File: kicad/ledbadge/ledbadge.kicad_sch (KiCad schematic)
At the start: 3 parts

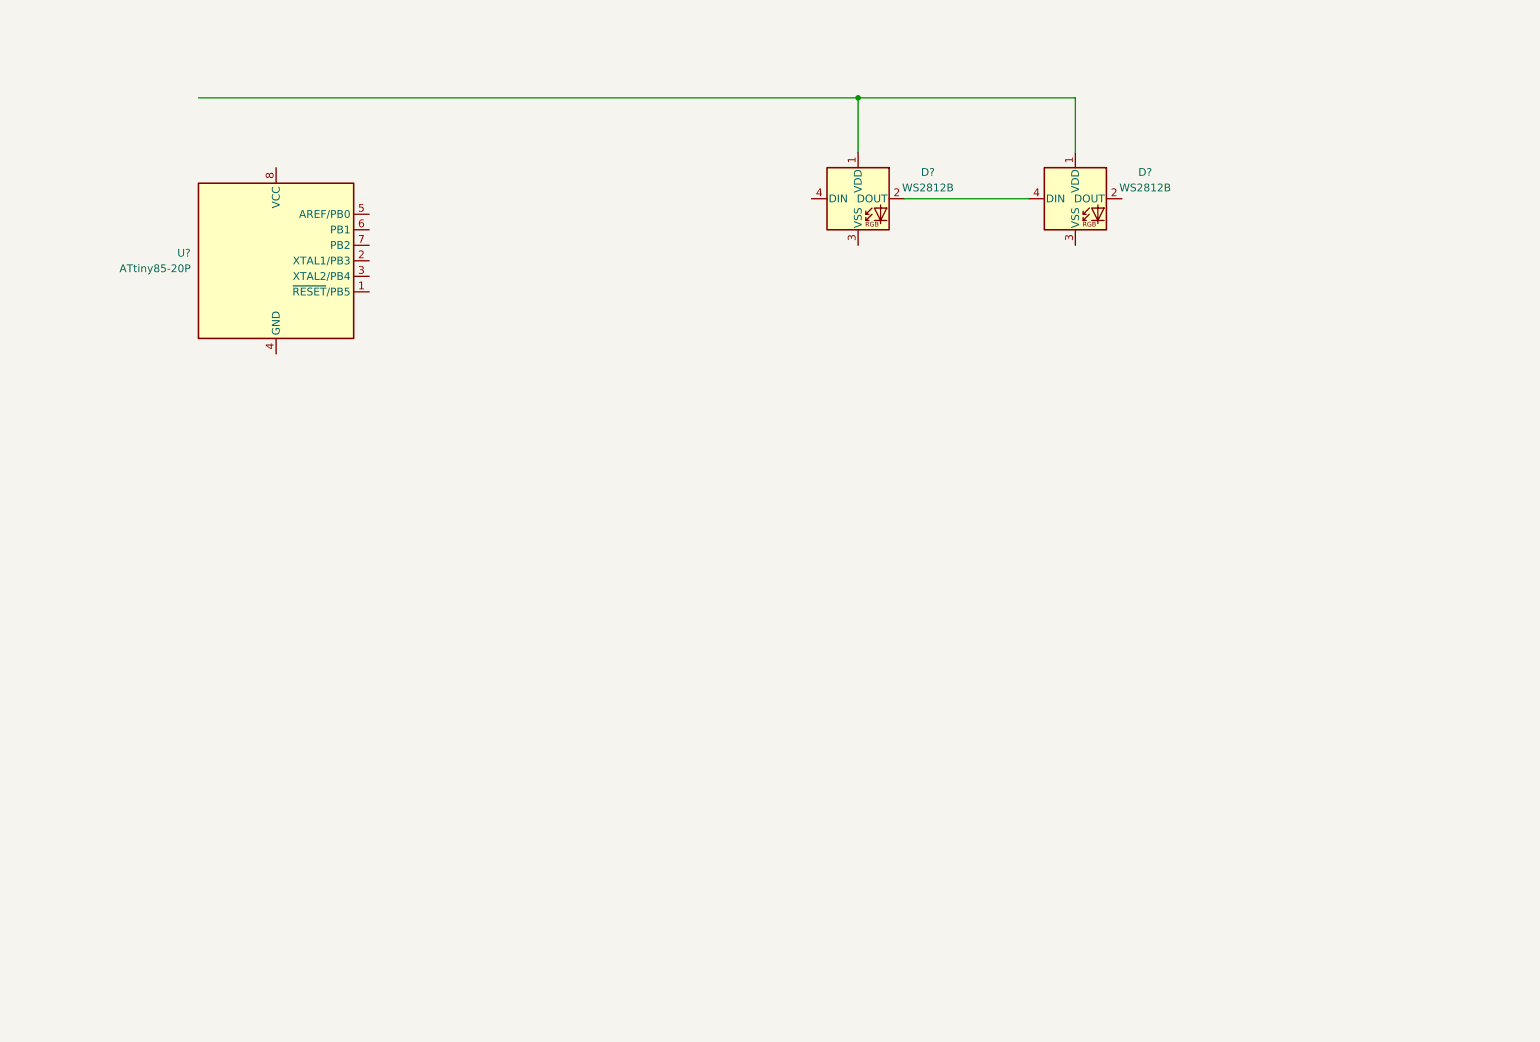
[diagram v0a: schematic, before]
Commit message: add a few more symbols, tidy up basic Readme added bypass capacitors and power symbols to the schematic
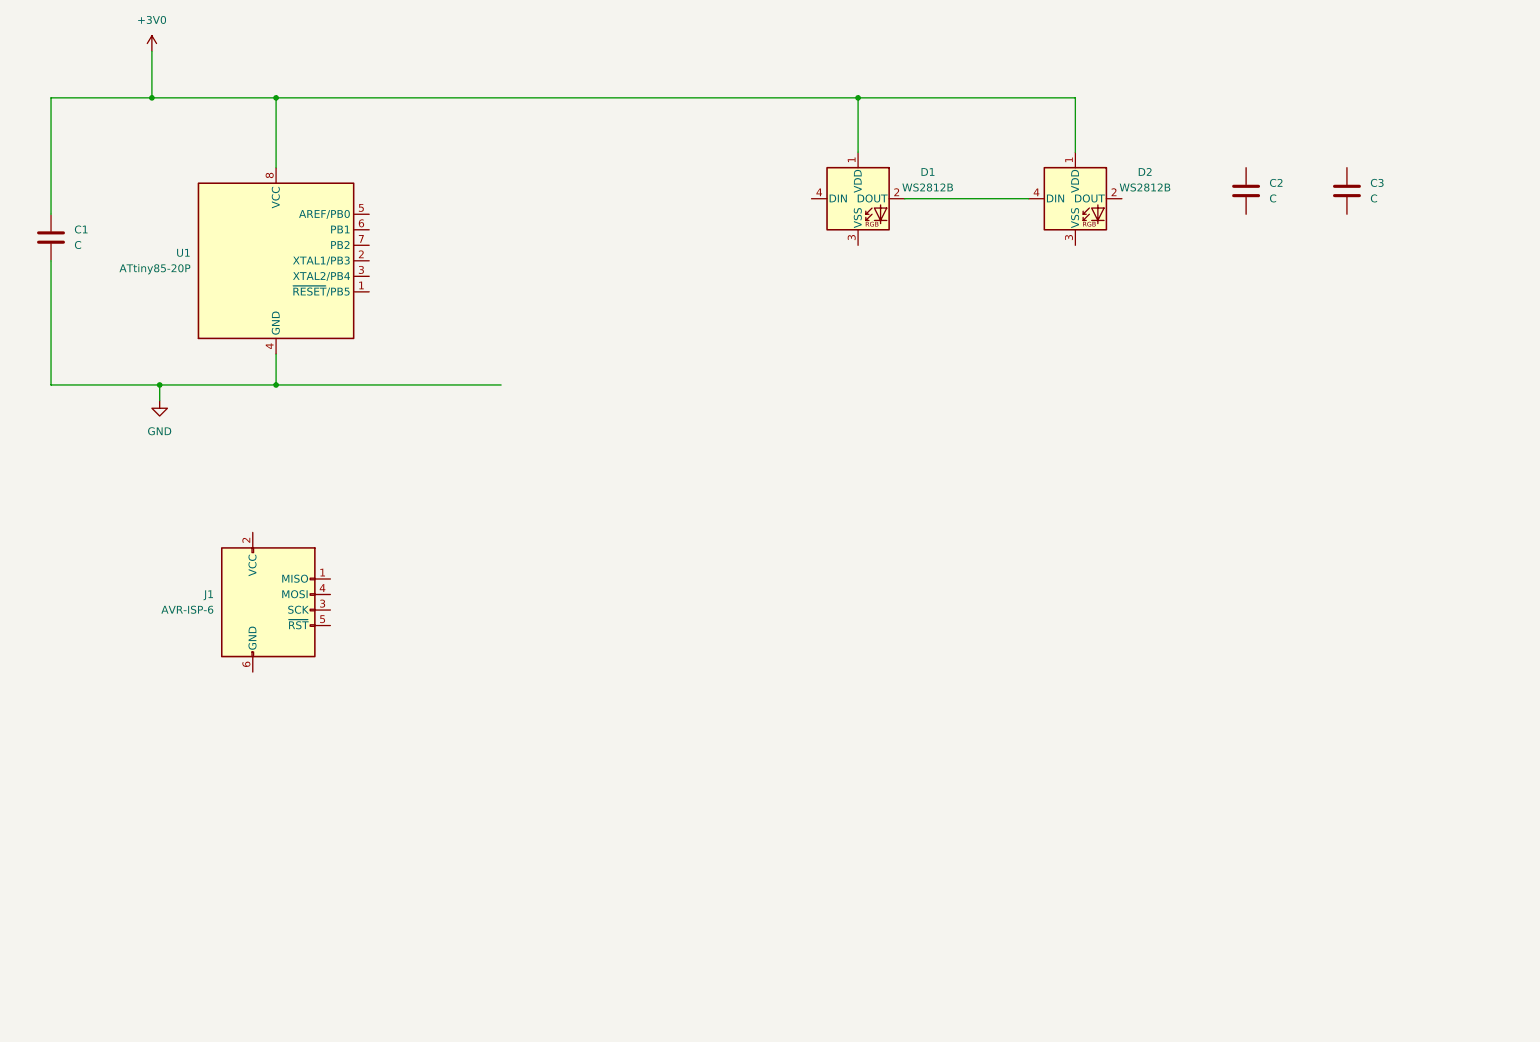
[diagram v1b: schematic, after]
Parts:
- added C1, C2, C3: C, symbol Device:C
- added J1: AVR-ISP-6, symbol Connector:AVR-ISP-6
- gave numbers to parts that had none: 3
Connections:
- net +3V0: now reaches D1.1 (VDD), D2.1 (VDD)
- net +3V0: now also U1.8 (VCC), C1.1
- net GND: now reaches U1.4 (GND)
- net GND: now also C1.2

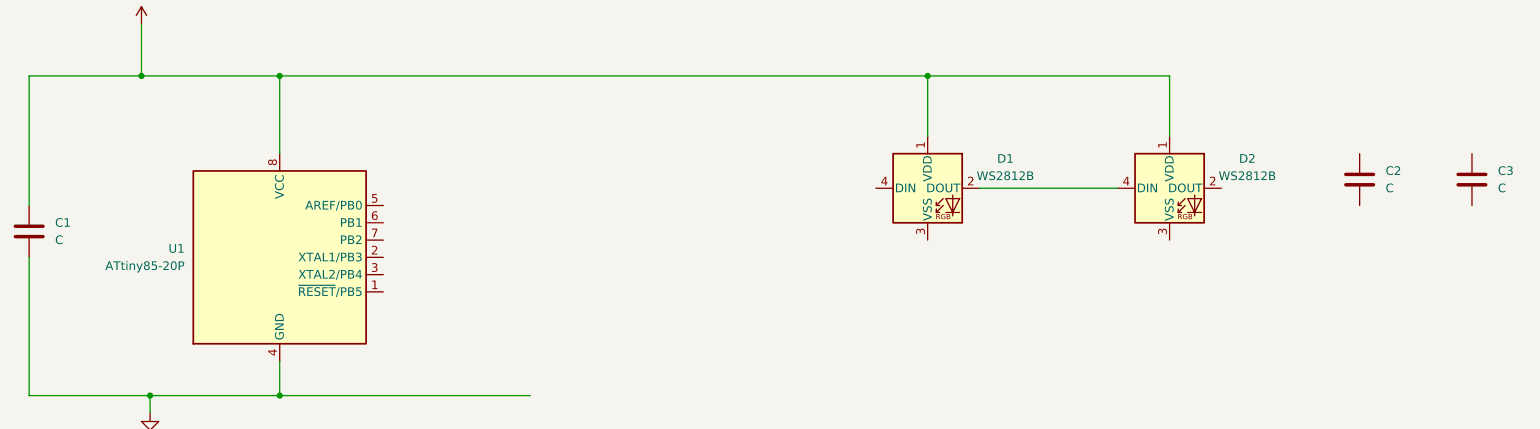
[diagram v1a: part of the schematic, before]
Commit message: add values to capacitors
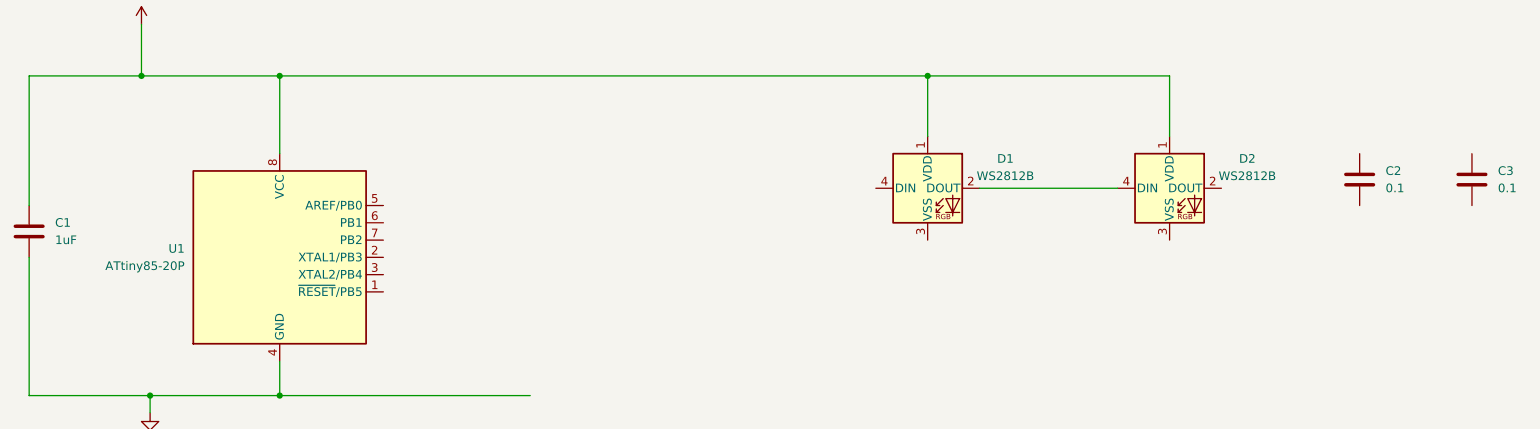
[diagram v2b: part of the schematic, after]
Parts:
- C1: value C -> 1uF
- C2, C3: value C -> 0.1
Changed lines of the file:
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@@
       (effects (font (size 1.27 1.27)) (justify left))
     )
-    (property "Value" "C" (at 231.14 57.15 0)
+    (property "Value" "0.1" (at 231.14 57.15 0)
       (effects (font (size 1.27 1.27)) (justify left))
     )
@@
       (effects (font (size 1.27 1.27)) (justify left))
     )
-    (property "Value" "C" (at 247.65 57.15 0)
+    (property "Value" "0.1" (at 247.65 57.15 0)
       (effects (font (size 1.27 1.27)) (justify left))
     )
@@
       (effects (font (size 1.27 1.27)) (justify left))
     )
-    (property "Value" "C" (at 35.56 64.77 0)
+    (property "Value" "1uF" (at 35.56 64.77 0)
       (effects (font (size 1.27 1.27)) (justify left))
     )

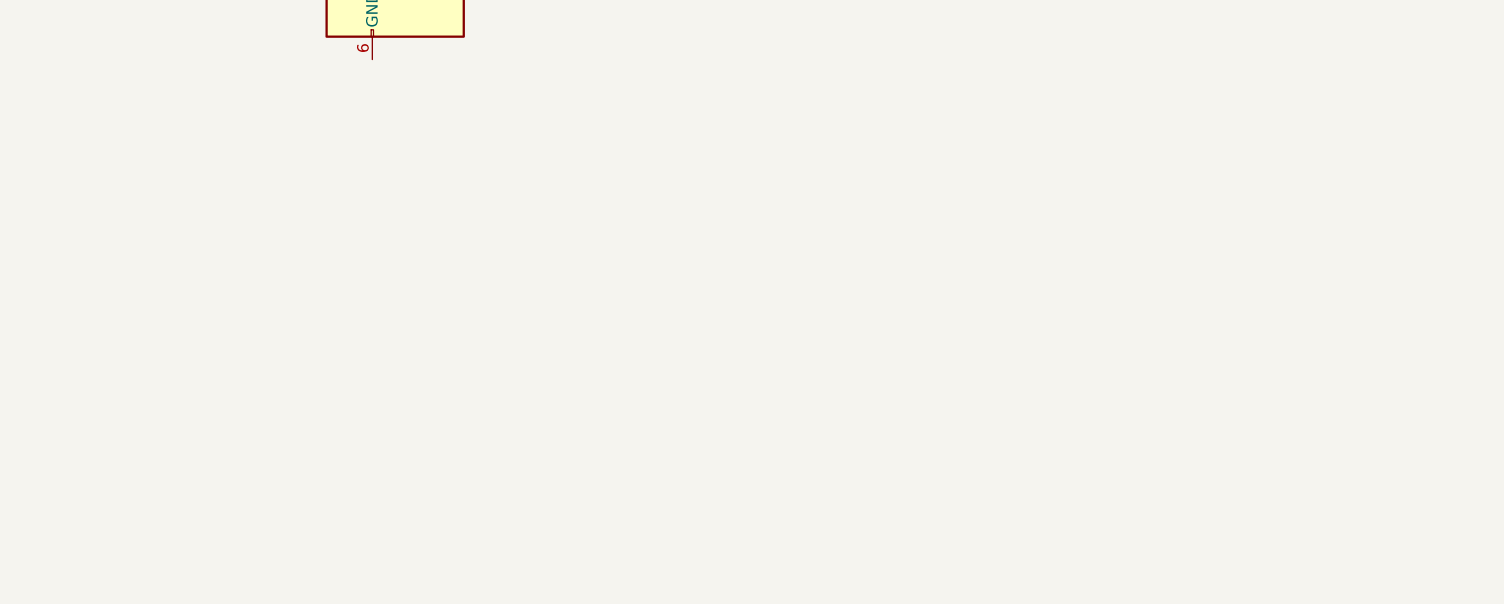
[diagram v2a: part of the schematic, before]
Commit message: add power input parts: battery, power switch
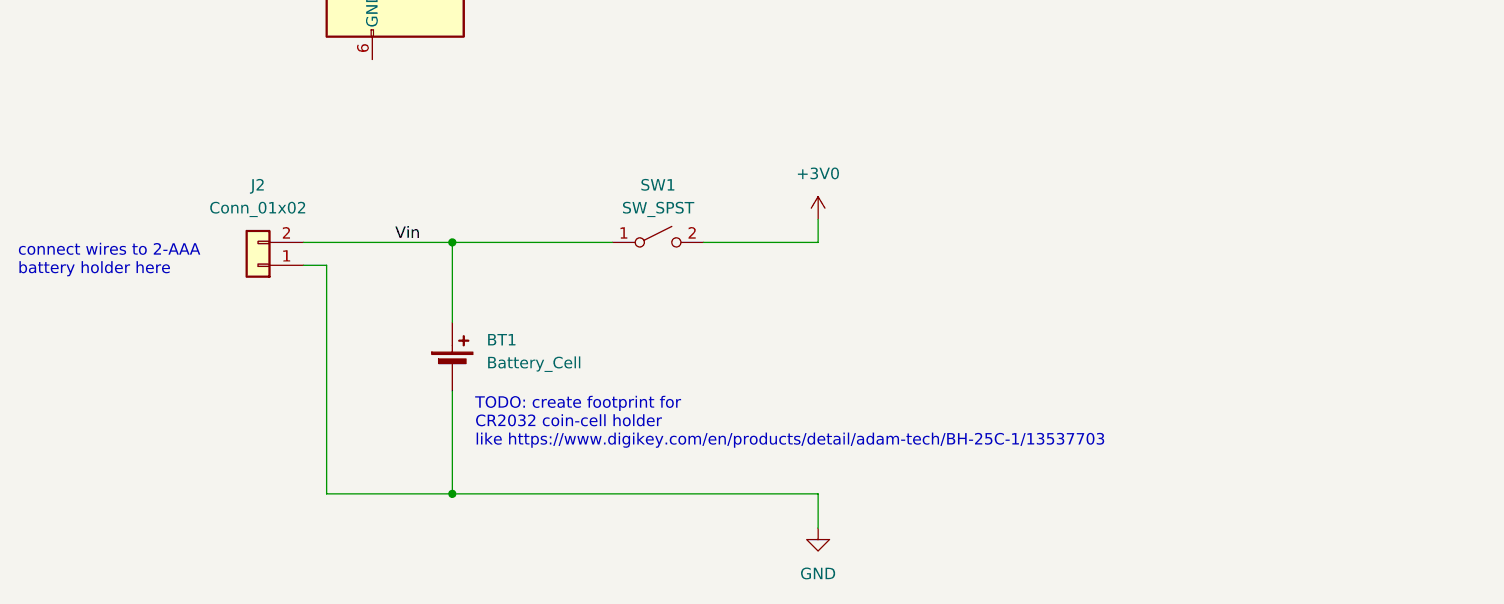
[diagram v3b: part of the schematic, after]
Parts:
- added BT1: Battery_Cell, symbol Device:Battery_Cell
- added J2: Conn_01x02, symbol Connector_Generic:Conn_01x02
- added SW1: SW_SPST, symbol Switch:SW_SPST
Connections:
- net +3V0: now also SW1.2 (B)
- net GND: now also BT1.2 (-), J2.1 (Pin_1)
- new net Vin: BT1.1 (+), J2.2 (Pin_2), SW1.1 (A)
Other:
- note added: "TODO: create footprint for CR2032 coin-cell holder like https://www.digikey.com/en/products/detail/adam-tech/BH-25C-1/13537703"
- note added: "connect wires to 2-AAA battery holder here"
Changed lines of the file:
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@@
 (kicad_sch (version 20230121) (generator eeschema)
   (paper "A4")
+  (junction (at 73.66 154.94) (diameter 0) (color 0 0 0 0)
+  )
   (junction (at 49.53 87.63) (diameter 0) (color 0 0 0 0)
   )
+  (junction (at 73.66 182.88) (diameter 0) (color 0 0 0 0)
+  )
   (junction (at 68.58 40.64) (diameter 0) (color 0 0 0 0)
   )
@@
   (junction (at 48.26 40.64) (diameter 0) (color 0 0 0 0)
   )
+  (wire (pts (xy 73.66 154.94) (xy 91.44 154.94))
+    (stroke (width 0) (type default))
+  )
   (wire (pts (xy 31.75 67.31) (xy 31.75 87.63))
     (stroke (width 0) (type default))
@@
     (stroke (width 0) (type default))
   )
+  (wire (pts (xy 73.66 182.88) (xy 114.3 182.88))
+    (stroke (width 0) (type default))
+  )
   (wire (pts (xy 31.75 87.63) (xy 49.53 87.63))
     (stroke (width 0) (type default))
@@
     (stroke (width 0) (type default))
   )
+  (wire (pts (xy 59.69 157.48) (xy 59.69 182.88))
+    (stroke (width 0) (type default))
+  )
   (wire (pts (xy 31.75 59.69) (xy 31.75 40.64))
     (stroke (width 0) (type default))
   )
+  (wire (pts (xy 73.66 171.45) (xy 73.66 182.88))
+    (stroke (width 0) (type default))
+  )
+  (wire (pts (xy 101.6 154.94) (xy 114.3 154.94))
+    (stroke (width 0) (type default))
+  )
   (wire (pts (xy 68.58 40.64) (xy 163.83 40.64))
     (stroke (width 0) (type default))
@@
     (stroke (width 0) (type default))
   )
+  (wire (pts (xy 114.3 152.4) (xy 114.3 154.94))
+    (stroke (width 0) (type default))
+  )
+  (wire (pts (xy 73.66 154.94) (xy 73.66 163.83))
+    (stroke (width 0) (type default))
+  )
   (wire (pts (xy 49.53 87.63) (xy 49.53 90.17))
     (stroke (width 0) (type default))
   )
+  (wire (pts (xy 57.15 157.48) (xy 59.69 157.48))
+    (stroke (width 0) (type default))
+  )
   (wire (pts (xy 199.39 49.53) (xy 199.39 40.64))
     (stroke (width 0) (type default))
@@
     (stroke (width 0) (type default))
   )
+  (wire (pts (xy 57.15 154.94) (xy 73.66 154.94))
+    (stroke (width 0) (type default))
+  )
   (wire (pts (xy 163.83 40.64) (xy 199.39 40.64))
     (stroke (width 0) (type default))
@@
     (stroke (width 0) (type default))
   )
+  (wire (pts (xy 114.3 182.88) (xy 114.3 186.69))
+    (stroke (width 0) (type default))
+  )
   (wire (pts (xy 171.45 57.15) (xy 191.77 57.15))
     (stroke (width 0) (type default))
   )
+  (wire (pts (xy 59.69 182.88) (xy 73.66 182.88))
+    (stroke (width 0) (type default))
+  )
   (wire (pts (xy 31.75 40.64) (xy 48.26 40.64))
     (stroke (width 0) (type default))
@@
   (wire (pts (xy 163.83 40.64) (xy 163.83 49.53))
     (stroke (width 0) (type default))
+  )
+  (text "TODO: create footprint for\nCR2032 coin-cell holder\nlike https://www.digikey.com/en/products/detail/adam-tech/BH-25C-1/13537703"
+    (at 76.2 177.8 0)
+    (effects (font (size 1.27 1.27)) (justify left bottom))
+  )
+  (text "connect wires to 2-AAA\nbattery holder here" (at 25.4 158.75 0)
+    (effects (font (size 1.27 1.27)) (justify left bottom))
+  )
+  (label "Vin" (at 67.31 154.94 0) (fields_autoplaced)
+    (effects (font (size 1.27 1.27)) (justify left bottom))
+  )
+  (symbol (lib_id "Connector_Generic:Conn_01x02") (at 52.07 157.48 180) (unit 1)
+    (in_bom yes) (on_board yes) (dnp no) (fields_autoplaced)
+    (property "Reference" "J2" (at 52.07 148.59 0)
+      (effects (font (size 1.27 1.27)))
+    )
+    (property "Value" "Conn_01x02" (at 52.07 151.13 0)
+      (effects (font (size 1.27 1.27)))
+    )
+    (property "Footprint" "" (at 52.07 157.48 0)
+      (effects (font (size 1.27 1.27)) hide)
+    )
+    (property "Datasheet" "~" (at 52.07 157.48 0)
+      (effects (font (size 1.27 1.27)) hide)
+    )
+    (pin "2")
+    (pin "1")
+    (instances
+      (project "ledbadge"
+        (path "/3a89a026-2e2f-4a4d-a795-8a4846df971d"
+          (reference "J2") (unit 1)
+        )
+      )
+    )
   )
   (symbol (lib_id "power:+3V0") (at 48.26 33.02 0) (unit 1)
@@
         (path "/3a89a026-2e2f-4a4d-a795-8a4846df971d"
           (reference "J1") (unit 1)
+        )
+      )
+    )
+  )
+  (symbol (lib_id "power:+3V0") (at 114.3 152.4 0) (unit 1)
+    (in_bom yes) (on_board yes) (dnp no) (fields_autoplaced)
+    (property "Reference" "#PWR03" (at 114.3 156.21 0)
+      (effects (font (size 1.27 1.27)) hide)
+    )
+    (property "Value" "+3V0" (at 114.3 147.32 0)
+      (effects (font (size 1.27 1.27)))
+    )
+    (property "Footprint" "" (at 114.3 152.4 0)
+      (effects (font (size 1.27 1.27)) hide)
+    )
+    (property "Datasheet" "" (at 114.3 152.4 0)
+      (effects (font (size 1.27 1.27)) hide)
+    )
+    (pin "1")
+    (instances
+      (project "ledbadge"
+        (path "/3a89a026-2e2f-4a4d-a795-8a4846df971d"
+          (reference "#PWR03") (unit 1)
+        )
+      )
+    )
+  )
+  (symbol (lib_id "Switch:SW_SPST") (at 96.52 154.94 0) (unit 1)
+    (in_bom yes) (on_board yes) (dnp no) (fields_autoplaced)
+    (property "Reference" "SW1" (at 96.52 148.59 0)
+      (effects (font (size 1.27 1.27)))
+    )
+    (property "Value" "SW_SPST" (at 96.52 151.13 0)
+      (effects (font (size 1.27 1.27)))
+    )
+    (property "Footprint" "" (at 96.52 154.94 0)
+      (effects (font (size 1.27 1.27)) hide)
+    )
+    (property "Datasheet" "~" (at 96.52 154.94 0)
+      (effects (font (size 1.27 1.27)) hide)
+    )
+    (pin "2")
+    (pin "1")
+    (instances
+      (project "ledbadge"
+        (path "/3a89a026-2e2f-4a4d-a795-8a4846df971d"
+          (reference "SW1") (unit 1)
         )
       )
@@
     )
   )
+  (symbol (lib_id "power:GND") (at 114.3 186.69 0) (unit 1)
+    (in_bom yes) (on_board yes) (dnp no) (fields_autoplaced)
+    (property "Reference" "#PWR04" (at 114.3 193.04 0)
+      (effects (font (size 1.27 1.27)) hide)
+    )
+    (property "Value" "GND" (at 114.3 191.77 0)
+      (effects (font (size 1.27 1.27)))
+    )
+    (property "Footprint" "" (at 114.3 186.69 0)
+      (effects (font (size 1.27 1.27)) hide)
+    )
+    (property "Datasheet" "" (at 114.3 186.69 0)
+      (effects (font (size 1.27 1.27)) hide)
+    )
+    (pin "1")
+    (instances
+      (project "ledbadge"
+        (path "/3a89a026-2e2f-4a4d-a795-8a4846df971d"
+          (reference "#PWR04") (unit 1)
+        )
+      )
+    )
+  )
   (symbol (lib_id "Device:C") (at 227.33 55.88 0) (unit 1)
     (in_bom yes) (on_board yes) (dnp no) (fields_autoplaced)
@@
         )
       )
+    )
+  )
+  (symbol (lib_id "Device:Battery_Cell") (at 73.66 168.91 0) (unit 1)
+    (in_bom yes) (on_board yes) (dnp no) (fields_autoplaced)
+    (property "Reference" "BT1" (at 77.47 165.7985 0)
+      (effects (font (size 1.27 1.27)) (justify left))
+    )
+    (property "Value" "Battery_Cell" (at 77.47 168.3385 0)
+      (effects (font (size 1.27 1.27)) (justify left))
+    )
+    (property "Footprint" "" (at 73.66 167.386 90)
+      (effects (font (size 1.27 1.27)) hide)
+    )
+    (property "Datasheet" "~" (at 73.66 167.386 90)
+      (effects (font (size 1.27 1.27)) hide)
+    )
+    (pin "2")
+    (pin "1")
+    (instances
+      (project "ledbadge"
+        (path "/3a89a026-2e2f-4a4d-a795-8a4846df971d"
+          (reference "BT1") (unit 1)
+        )
+      )
